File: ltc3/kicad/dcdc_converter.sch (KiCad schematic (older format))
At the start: 18 parts, among them U3 PTN78020W

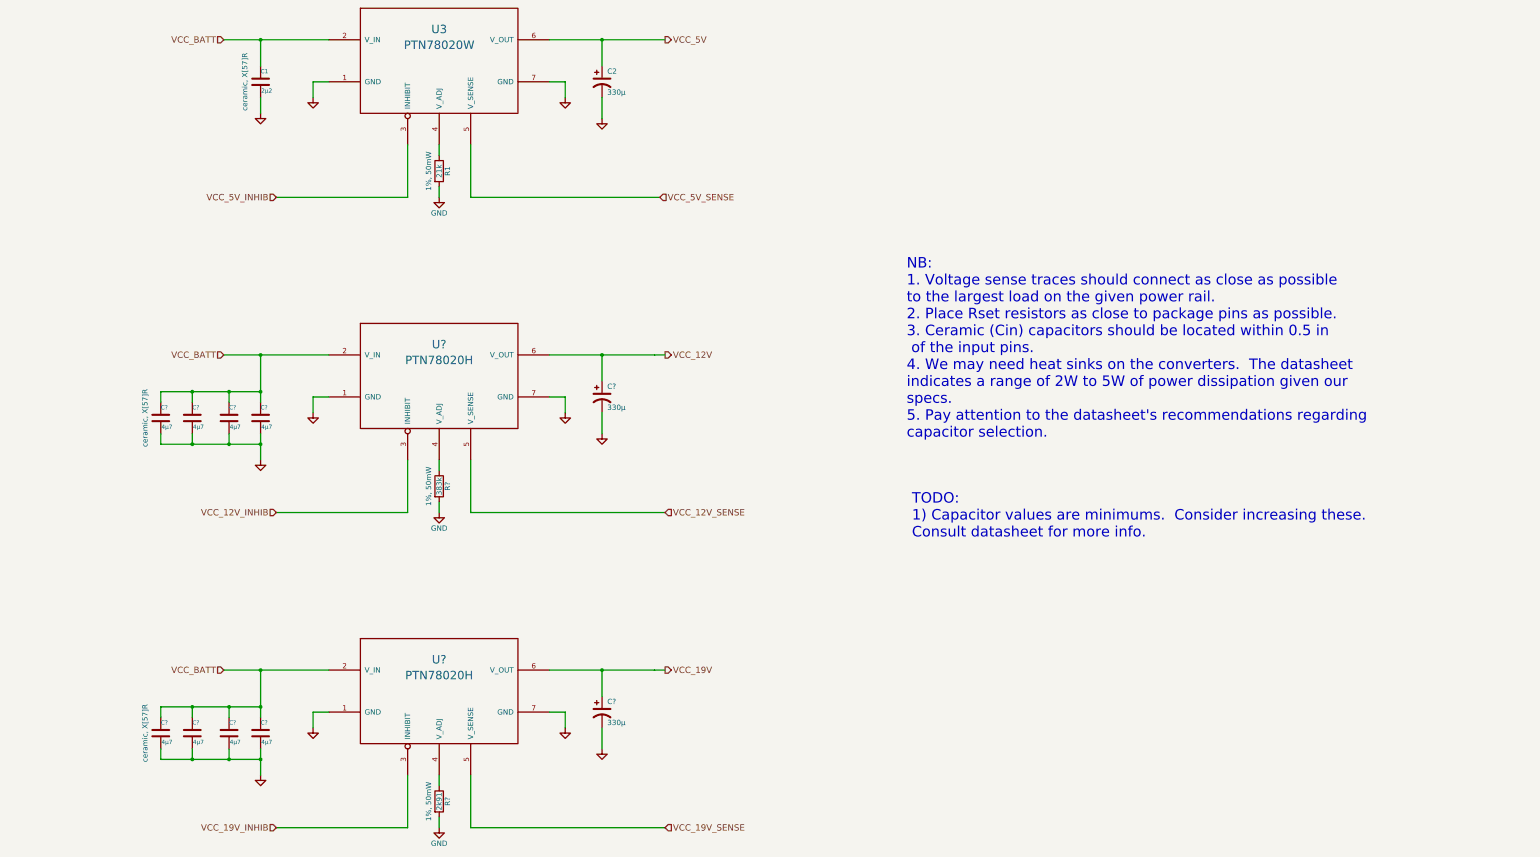
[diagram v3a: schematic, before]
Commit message: A bit of progress on the LTC3 power-monitoring hardware.
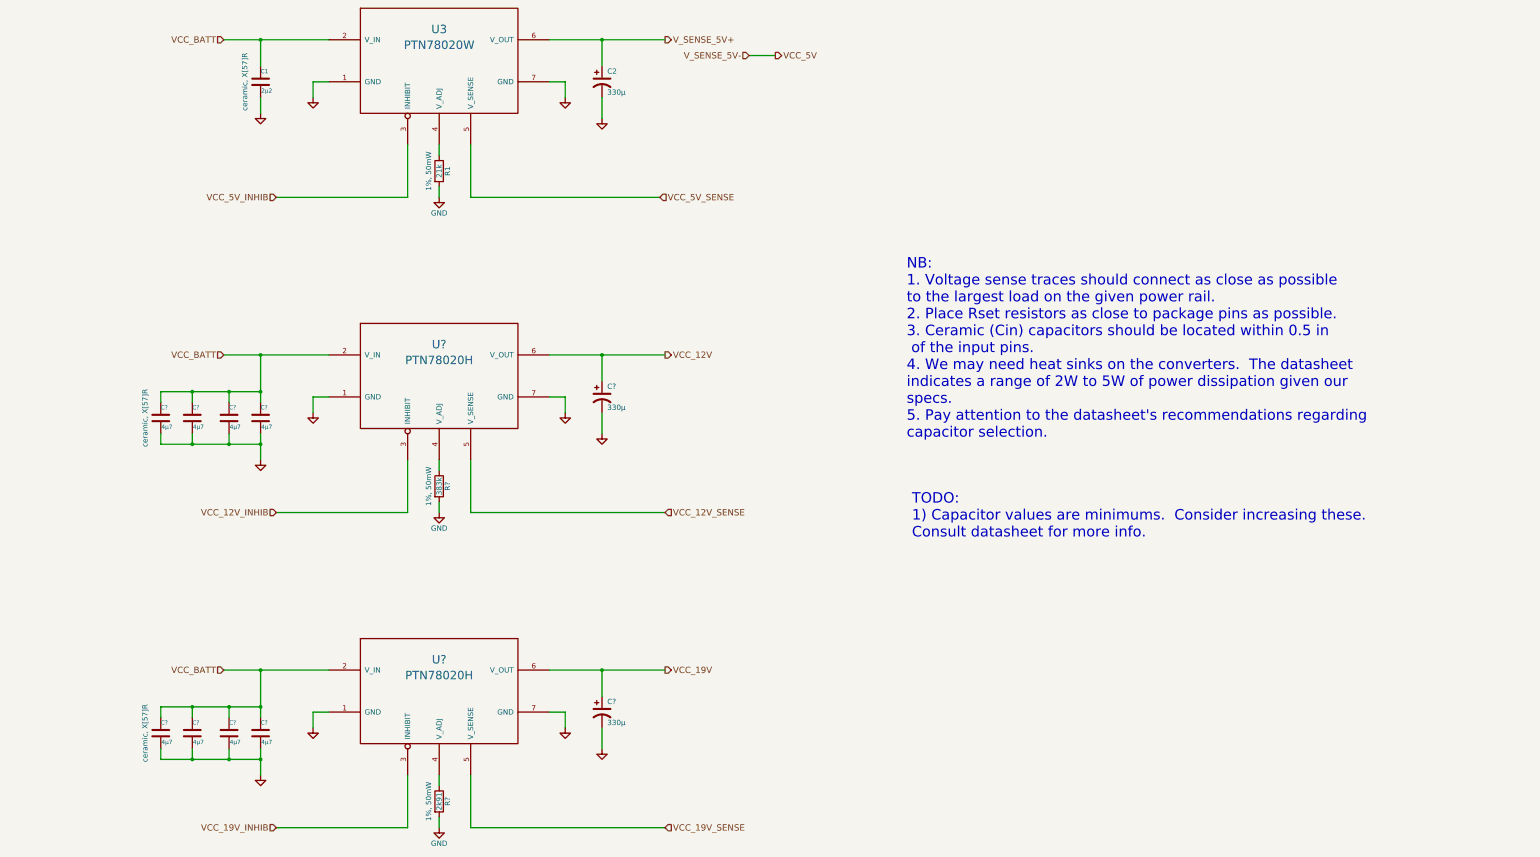
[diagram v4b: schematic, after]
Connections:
- net VCC_5V: no longer C2.1, U3.6 (V_OUT)
- new net V_SENSE_5V+: C2.1, U3.6 (V_OUT)
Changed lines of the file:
@@
 $Descr B 17000 11000
 encoding utf-8
-Sheet 3 7
+Sheet 7 7
 Title "LTC3 12V-to-5V DC/DC Converter"
 Date "30 may 2015"
@@
 Comment4 ""
 $EndDescr
-Text HLabel 8150 1800 2    60   Output ~ 0
+Text HLabel 9200 1950 2    60   Output ~ 0
 VCC_5V
 Text HLabel 3950 1800 0    60   Input ~ 0
@@
 	1    0    0    -1
 $EndComp
-Wire Wire Line
-	4950 2200 4800 2200
-Wire Wire Line
-	4800 2200 4800 2350
-Wire Wire Line
-	7050 2200 7200 2200
-Wire Wire Line
-	7200 2200 7200 2350
-Wire Wire Line
-	7050 1800 7550 1800
-Wire Wire Line
-	7550 1800 8150 1800
-Wire Wire Line
-	3950 1800 4300 1800
-Wire Wire Line
-	4300 1800 4950 1800
 $Comp
 L CP1 C2
@@
 	1    0    0    -1
 $EndComp
-Wire Wire Line
-	7550 2050 7550 1800
-Connection ~ 7550 1800
-Wire Wire Line
-	7550 2350 7550 2550
 $Comp
 L C C1
@@
 	1    0    0    -1
 $EndComp
-Wire Wire Line
-	4300 2500 4300 2350
-Wire Wire Line
-	4300 2050 4300 1800
-Connection ~ 4300 1800
 $Comp
 L R R1
@@
 	1    0    0    -1
 $EndComp
-Wire Wire Line
-	6000 3300 6000 3200
-Wire Wire Line
-	6000 2900 6000 2800
 Text HLabel 4450 3300 0    60   Input ~ 0
 VCC_5V_INHIB
-Wire Wire Line
-	5700 2800 5700 3300
-Wire Wire Line
-	5700 3300 4450 3300
-Wire Wire Line
-	6300 2800 6300 3300
-Wire Wire Line
-	6300 3300 8100 3300
 Text HLabel 8150 4800 2    60   Output ~ 0
 VCC_12V
@@
 	1    0    0    -1
 $EndComp
-Wire Wire Line
-	4950 5200 4800 5200
-Wire Wire Line
-	4800 5200 4800 5350
-Wire Wire Line
-	7050 5200 7200 5200
-Wire Wire Line
-	7200 5200 7200 5350
-Wire Wire Line
-	7050 4800 7550 4800
-Wire Wire Line
-	7550 4800 8050 4800
-Wire Wire Line
-	8050 4800 8150 4800
-Wire Wire Line
-	3950 4800 4300 4800
-Wire Wire Line
-	4300 4800 4950 4800
 $Comp
 L CP1 C?
@@
 	1    0    0    -1
 $EndComp
-Wire Wire Line
-	7550 5050 7550 4800
-Connection ~ 7550 4800
-Wire Wire Line
-	7550 5350 7550 5550
 $Comp
 L C C?
@@
 	1    0    0    -1
 $EndComp
-Wire Wire Line
-	4300 5800 4300 5650
-Wire Wire Line
-	4300 5650 4300 5550
-Wire Wire Line
-	4300 4800 4300 5150
-Wire Wire Line
-	4300 5150 4300 5250
-Connection ~ 4300 4800
 $Comp
 L R R?
@@
 	1    0    0    -1
 $EndComp
-Wire Wire Line
-	6000 6300 6000 6200
-Wire Wire Line
-	6000 5900 6000 5800
 Text HLabel 4450 6300 0    60   Input ~ 0
 VCC_12V_INHIB
-Wire Wire Line
-	5700 5800 5700 6300
-Wire Wire Line
-	5700 6300 4450 6300
-Wire Wire Line
-	6300 5800 6300 6300
-Wire Wire Line
-	6300 6300 8150 6300
 Text HLabel 8150 7800 2    60   Output ~ 0
 VCC_19V
@@
 	1    0    0    -1
 $EndComp
-Wire Wire Line
-	4950 8200 4800 8200
-Wire Wire Line
-	4800 8200 4800 8350
-Wire Wire Line
-	7050 8200 7200 8200
-Wire Wire Line
-	7200 8200 7200 8350
-Wire Wire Line
-	7050 7800 7550 7800
-Wire Wire Line
-	7550 7800 8050 7800
-Wire Wire Line
-	8050 7800 8150 7800
-Wire Wire Line
-	3950 7800 4300 7800
-Wire Wire Line
-	4300 7800 4950 7800
 $Comp
 L CP1 C?
@@
 	1    0    0    -1
 $EndComp
-Wire Wire Line
-	7550 8050 7550 7800
-Connection ~ 7550 7800
-Wire Wire Line
-	7550 8350 7550 8550
-Connection ~ 4300 7800
 $Comp
 L R R?
@@
 	1    0    0    -1
 $EndComp
-Wire Wire Line
-	6000 9300 6000 9200
-Wire Wire Line
-	6000 8900 6000 8800
 Text HLabel 4450 9300 0    60   Input ~ 0
 VCC_19V_INHIB
-Wire Wire Line
-	5700 8800 5700 9300
-Wire Wire Line
-	5700 9300 4450 9300
-Wire Wire Line
-	6300 8800 6300 9300
-Wire Wire Line
-	6300 9300 8150 9300
 Text Notes 10450 5600 0    100  ~ 0
 NB:\n1. Voltage sense traces should connect as close as possible\nto the largest load on the given power rail.\n2. Place Rset resistors as close to package pins as possible.\n3. Ceramic (Cin) capacitors should be located within 0.5 in\n of the input pins.\n4. We may need heat sinks on the converters.  The datasheet\nindicates a range of 2W to 5W of power dissipation given our\nspecs.\n5. Pay attention to the datasheet's recommendations regarding\ncapacitor selection.
@@
 	1    0    0    -1
 $EndComp
-Wire Wire Line
-	4000 5150 4000 5250
-Wire Wire Line
-	3350 5150 3650 5150
-Wire Wire Line
-	3650 5150 4000 5150
-Wire Wire Line
-	4000 5150 4300 5150
-Connection ~ 4300 5150
-Wire Wire Line
-	3650 5250 3650 5150
-Connection ~ 4000 5150
-Wire Wire Line
-	3350 5250 3350 5150
-Connection ~ 3650 5150
-Wire Wire Line
-	4000 5550 4000 5650
-Wire Wire Line
-	3350 5650 3650 5650
-Wire Wire Line
-	3650 5650 4000 5650
-Wire Wire Line
-	4000 5650 4300 5650
-Connection ~ 4300 5650
-Wire Wire Line
-	3650 5550 3650 5650
-Connection ~ 4000 5650
-Wire Wire Line
-	3350 5550 3350 5650
-Connection ~ 3650 5650
 $Comp
 L C C?
@@
 	1    0    0    -1
 $EndComp
-Wire Wire Line
-	4300 8800 4300 8650
-Wire Wire Line
-	4300 8650 4300 8550
-Wire Wire Line
-	4300 7800 4300 8150
-Wire Wire Line
-	4300 8150 4300 8250
 $Comp
 L C C?
@@
 	1    0    0    -1
 $EndComp
-Wire Wire Line
-	4000 8150 4000 8250
-Wire Wire Line
-	3350 8150 3650 8150
-Wire Wire Line
-	3650 8150 4000 8150
-Wire Wire Line
-	4000 8150 4300 8150
-Connection ~ 4300 8150
-Wire Wire Line
-	3650 8250 3650 8150
-Connection ~ 4000 8150
-Wire Wire Line
-	3350 8250 3350 8150
-Connection ~ 3650 8150
-Wire Wire Line
-	4000 8550 4000 8650
-Wire Wire Line
-	3350 8650 3650 8650
-Wire Wire Line
-	3650 8650 4000 8650
-Wire Wire Line
-	4000 8650 4300 8650
-Connection ~ 4300 8650
-Wire Wire Line
-	3650 8550 3650 8650
-Connection ~ 4000 8650
-Wire Wire Line
-	3350 8550 3350 8650
-Connection ~ 3650 8650
 Text Notes 10500 6550 0    100  ~ 0
 TODO:\n1) Capacitor values are minimums.  Consider increasing these.\nConsult datasheet for more info.
@@
 Text HLabel 8150 9300 2    60   Input ~ 0
 VCC_19V_SENSE
+Text HLabel 8150 1800 2    60   Output ~ 0
+V_SENSE_5V+
+Text HLabel 8950 1950 0    60   Input ~ 0
+V_SENSE_5V-
+Wire Wire Line
+	4950 2200 4800 2200
+Wire Wire Line
+	4800 2200 4800 2350
+Wire Wire Line
+	7050 2200 7200 2200
+Wire Wire Line
+	7200 2200 7200 2350
+Wire Wire Line
+	7050 1800 8150 1800
+Wire Wire Line
+	3950 1800 4950 1800
+Wire Wire Line
+	7550 2050 7550 1800
+Connection ~ 7550 1800
+Wire Wire Line
+	7550 2350 7550 2550
+Wire Wire Line
+	4300 2500 4300 2350
+Wire Wire Line
+	4300 2050 4300 1800
+Connection ~ 4300 1800
+Wire Wire Line
+	6000 3300 6000 3200
+Wire Wire Line
+	6000 2900 6000 2800
+Wire Wire Line
+	5700 2800 5700 3300
+Wire Wire Line
+	5700 3300 4450 3300
+Wire Wire Line
+	6300 2800 6300 3300
+Wire Wire Line
+	6300 3300 8100 3300
+Wire Wire Line
+	4950 5200 4800 5200
+Wire Wire Line
+	4800 5200 4800 5350
+Wire Wire Line
+	7050 5200 7200 5200
+Wire Wire Line
+	7200 5200 7200 5350
+Wire Wire Line
+	7050 4800 8150 4800
+Wire Wire Line
+	3950 4800 4950 4800
+Wire Wire Line
+	7550 5050 7550 4800
+Connection ~ 7550 4800
+Wire Wire Line
+	7550 5350 7550 5550
+Wire Wire Line
+	4300 5550 4300 5800
+Wire Wire Line
+	4300 4800 4300 5250
+Connection ~ 4300 4800
+Wire Wire Line
+	6000 6300 6000 6200
+Wire Wire Line
+	6000 5900 6000 5800
+Wire Wire Line
+	5700 5800 5700 6300
+Wire Wire Line
+	5700 6300 4450 6300
+Wire Wire Line
+	6300 5800 6300 6300
+Wire Wire Line
+	6300 6300 8150 6300
+Wire Wire Line
+	4950 8200 4800 8200
+Wire Wire Line
+	4800 8200 4800 8350
+Wire Wire Line
+	7050 8200 7200 8200
+Wire Wire Line
+	7200 8200 7200 8350
+Wire Wire Line
+	7050 7800 8150 7800
+Wire Wire Line
+	3950 7800 4950 7800
+Wire Wire Line
+	7550 8050 7550 7800
+Connection ~ 7550 7800
+Wire Wire Line
+	7550 8350 7550 8550
+Connection ~ 4300 7800
+Wire Wire Line
+	6000 9300 6000 9200
+Wire Wire Line
+	6000 8900 6000 8800
+Wire Wire Line
+	5700 8800 5700 9300
+Wire Wire Line
+	5700 9300 4450 9300
+Wire Wire Line
+	6300 8800 6300 9300
+Wire Wire Line
+	6300 9300 8150 9300
+Wire Wire Line
+	4000 5150 4000 5250
+Wire Wire Line
+	3350 5150 4300 5150
+Connection ~ 4300 5150
+Wire Wire Line
+	3650 5250 3650 5150
+Connection ~ 4000 5150
+Wire Wire Line
+	3350 5250 3350 5150
+Connection ~ 3650 5150
+Wire Wire Line
+	4000 5650 4000 5550
+Wire Wire Line
+	3350 5650 4300 5650
+Connection ~ 4300 5650
+Wire Wire Line
+	3650 5550 3650 5650
+Connection ~ 4000 5650
+Wire Wire Line
+	3350 5550 3350 5650
+Connection ~ 3650 5650
+Wire Wire Line
+	4300 8550 4300 8800
+Wire Wire Line
+	4300 7800 4300 8250
+Wire Wire Line
+	4000 8150 4000 8250
+Wire Wire Line
+	3350 8150 4300 8150
+Connection ~ 4300 8150
+Wire Wire Line
+	3650 8250 3650 8150
+Connection ~ 4000 8150
+Wire Wire Line
+	3350 8250 3350 8150
+Connection ~ 3650 8150
+Wire Wire Line
+	4000 8650 4000 8550
+Wire Wire Line
+	3350 8650 4300 8650
+Connection ~ 4300 8650
+Wire Wire Line
+	3650 8550 3650 8650
+Connection ~ 4000 8650
+Wire Wire Line
+	3350 8550 3350 8650
+Connection ~ 3650 8650
+Wire Wire Line
+	8950 1950 9200 1950
 $EndSCHEMATC

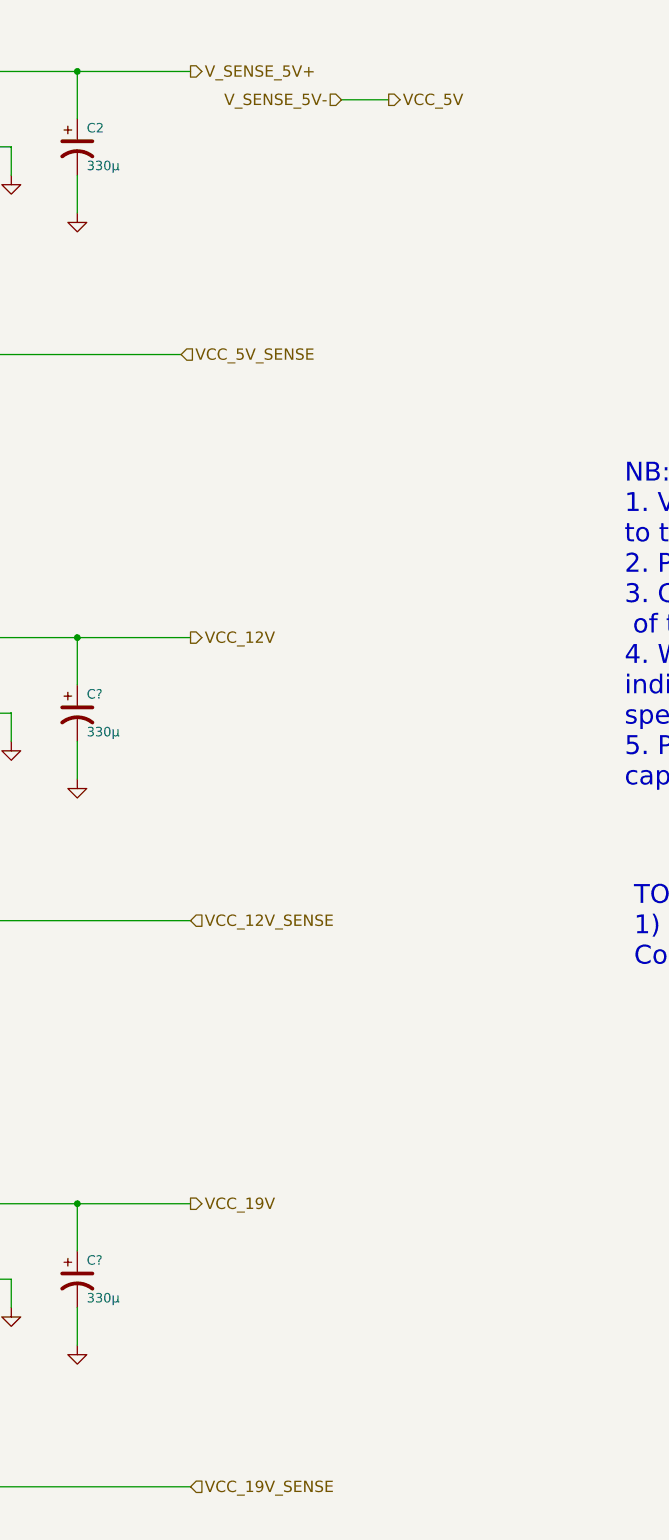
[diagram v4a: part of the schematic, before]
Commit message: More work on power sensors. Beginning to wire up the DC-DC Converter sheet with the BeagleBone Cape sheet.
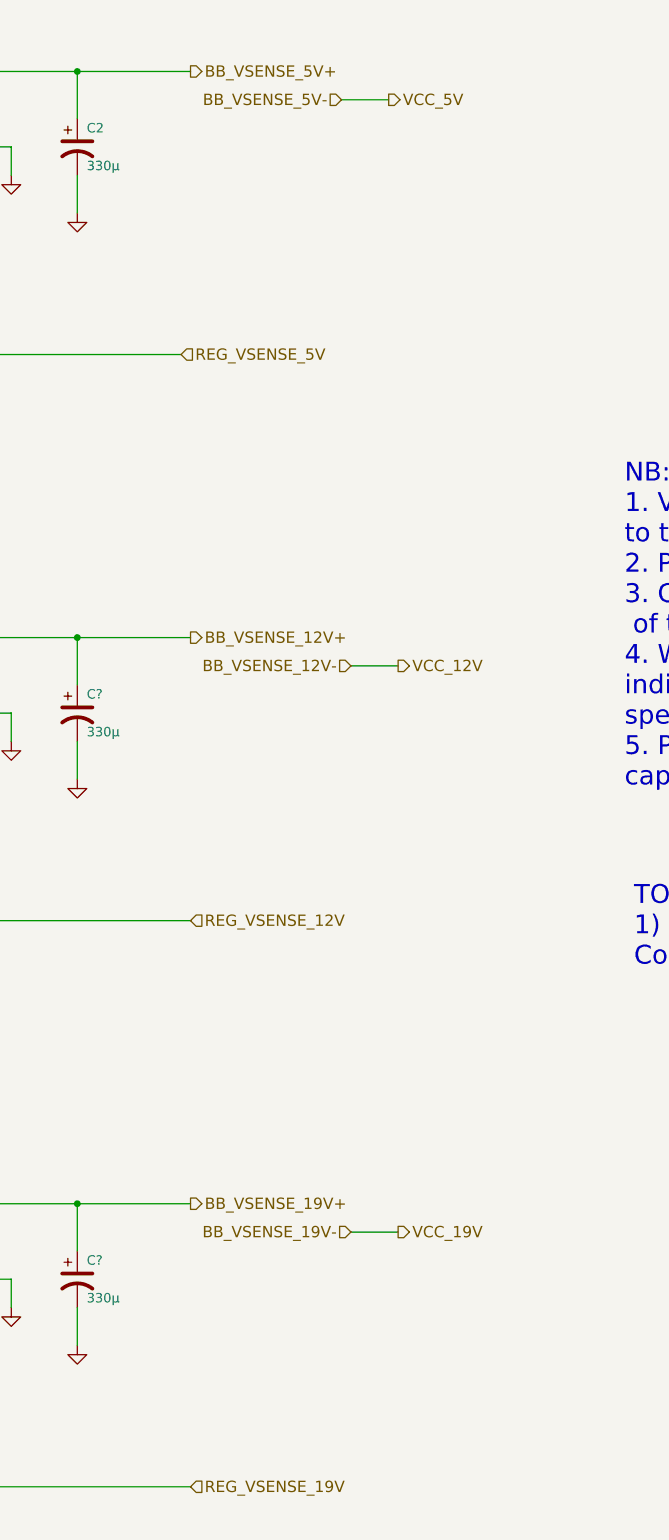
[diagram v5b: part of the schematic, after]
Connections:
- net VCC_12V renamed BB_VSENSE_12V+
- net VCC_12V_SENSE renamed REG_VSENSE_12V
- net VCC_19V renamed BB_VSENSE_19V+
- net VCC_19V_SENSE renamed REG_VSENSE_19V
- net VCC_5V_SENSE renamed REG_VSENSE_5V
- net V_SENSE_5V+ renamed BB_VSENSE_5V+
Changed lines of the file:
@@
 VCC_5V_INHIB
 Text HLabel 8150 4800 2    60   Output ~ 0
-VCC_12V
+BB_VSENSE_12V+
 Text HLabel 3950 4800 0    60   Input ~ 0
 VCC_BATT
@@
 VCC_12V_INHIB
 Text HLabel 8150 7800 2    60   Output ~ 0
-VCC_19V
+BB_VSENSE_19V+
 Text HLabel 3950 7800 0    60   Input ~ 0
 VCC_BATT
@@
 TODO:\n1) Capacitor values are minimums.  Consider increasing these.\nConsult datasheet for more info.
 Text HLabel 8100 3300 2    60   Input ~ 0
-VCC_5V_SENSE
+REG_VSENSE_5V
 Text HLabel 8150 6300 2    60   Input ~ 0
-VCC_12V_SENSE
+REG_VSENSE_12V
 Text HLabel 8150 9300 2    60   Input ~ 0
-VCC_19V_SENSE
+REG_VSENSE_19V
 Text HLabel 8150 1800 2    60   Output ~ 0
-V_SENSE_5V+
+BB_VSENSE_5V+
 Text HLabel 8950 1950 0    60   Input ~ 0
-V_SENSE_5V-
+BB_VSENSE_5V-
 Wire Wire Line
 	4950 2200 4800 2200
@@
 Wire Wire Line
 	8950 1950 9200 1950
+Text HLabel 9250 4950 2    60   Output ~ 0
+VCC_12V
+Text HLabel 9000 4950 0    60   Input ~ 0
+BB_VSENSE_12V-
+Wire Wire Line
+	9000 4950 9250 4950
+Text HLabel 9250 7950 2    60   Output ~ 0
+VCC_19V
+Text HLabel 9000 7950 0    60   Input ~ 0
+BB_VSENSE_19V-
+Wire Wire Line
+	9000 7950 9250 7950
 $EndSCHEMATC
